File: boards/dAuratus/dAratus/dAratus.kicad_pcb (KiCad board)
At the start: 2 copper layers, 11 parts, among them SW1 SW_SPDT, U1 ADP7104ARDZ, U2 AVR128DB28-SOIC

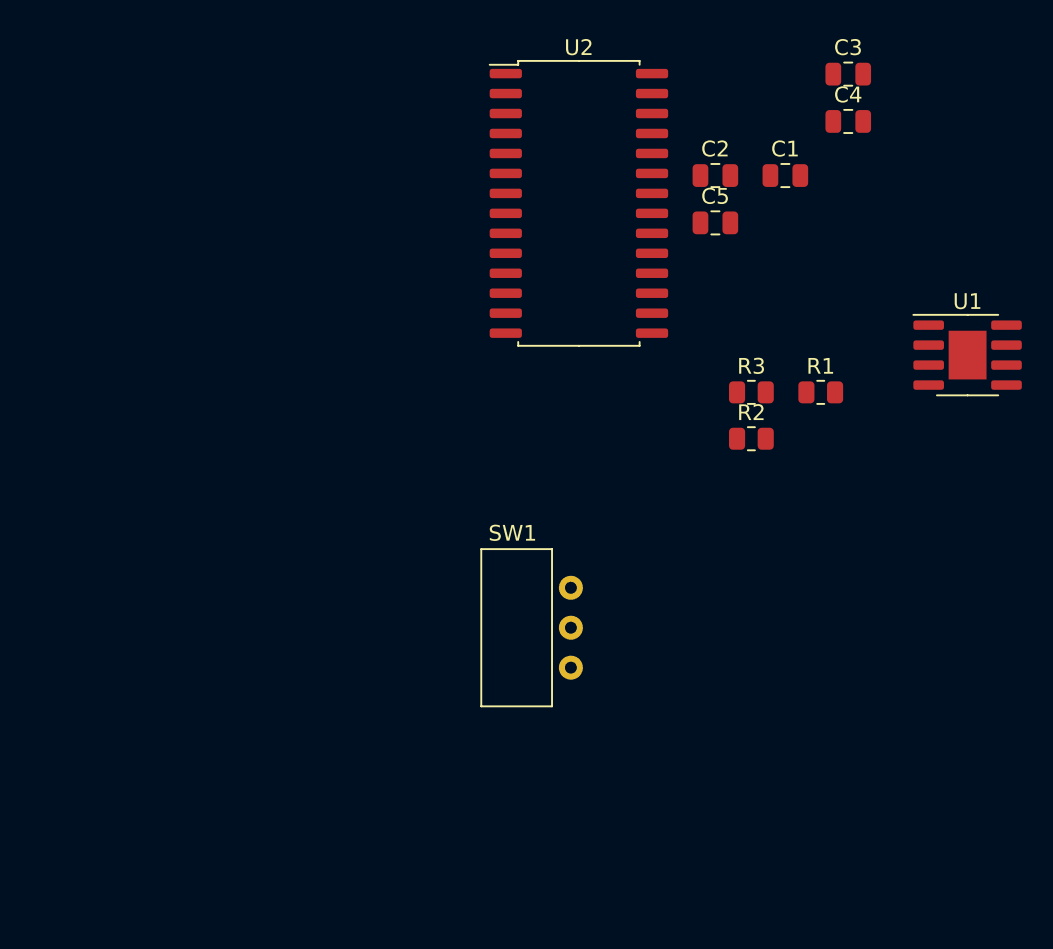
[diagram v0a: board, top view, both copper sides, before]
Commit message: Version 1.0 of fan control software.
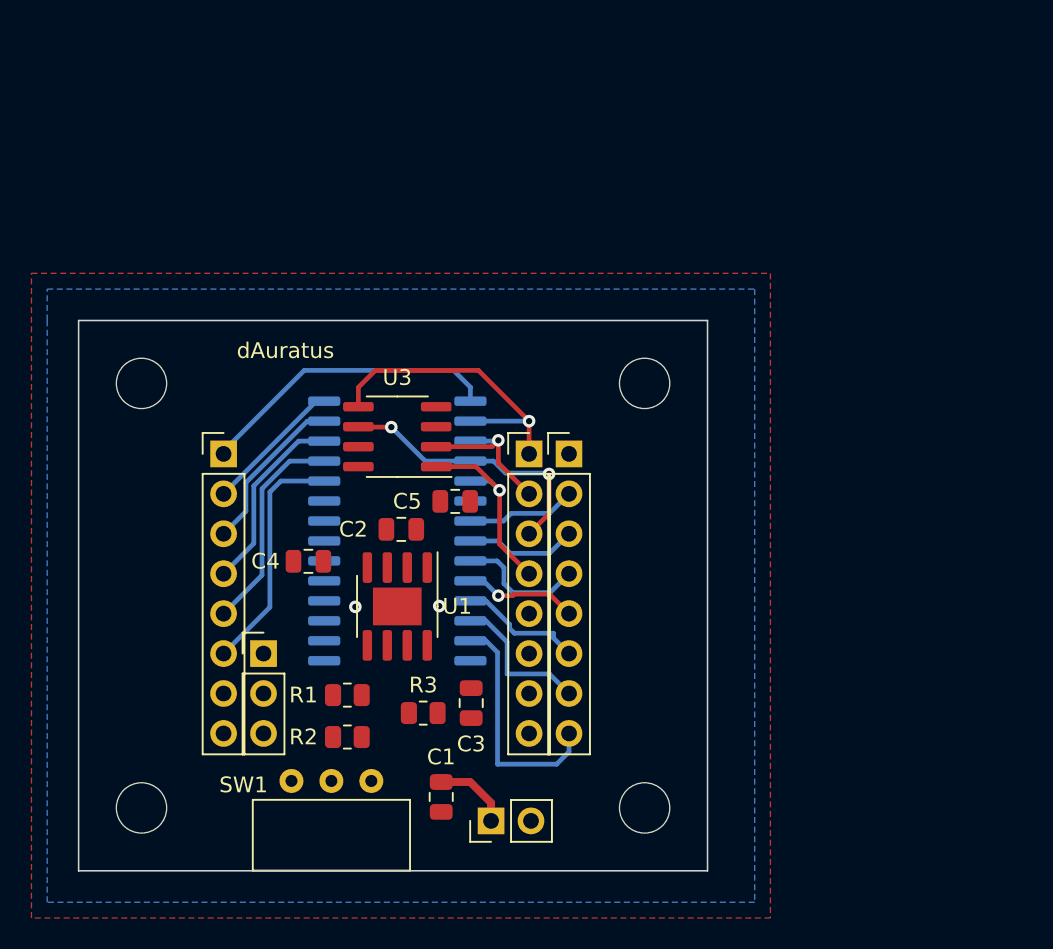
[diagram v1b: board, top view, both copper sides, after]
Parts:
- added H1: MountingHole, MountingHole:MountingHole_3.2mm_M3, F.Cu at (104.0, 104.0)
- added H2: MountingHole, MountingHole:MountingHole_3.2mm_M3, F.Cu at (136.0, 104.0)
- added H3: MountingHole, MountingHole:MountingHole_3.2mm_M3, F.Cu at (104.0, 131.0)
- added H4: MountingHole, MountingHole:MountingHole_3.2mm_M3, F.Cu at (136.0, 131.0)
- added J1: Conn_01x03_Male, Connector_PinHeader_2.54mm:PinHeader_1x03_P2.54mm_Vertical, F.Cu at (111.8, 121.2)
- added J2: Conn_01x08_Female, Connector_PinHeader_2.54mm:PinHeader_1x08_P2.54mm_Vertical, F.Cu at (131.2, 108.5)
- added J3: Conn_01x08_Female, Connector_PinHeader_2.54mm:PinHeader_1x08_P2.54mm_Vertical, F.Cu at (109.2, 108.5)
- added J4: Conn_01x08_Female, Connector_PinHeader_2.54mm:PinHeader_1x08_P2.54mm_Vertical, F.Cu at (128.7, 108.5)
- added J5: Conn_01x02_Male, Connector_PinHeader_2.54mm:PinHeader_1x02_P2.54mm_Vertical, F.Cu at (126.2, 131.8)
- added U3: AT25xxx, Package_SO:SOIC-8_3.9x4.9mm_P1.27mm, F.Cu at (120.3, 107.4)
- U2: moved to B.Cu
- moved C3 46.6 mm to (125.0, 124.3), turned to -90 degrees
- moved C1 45.2 mm to (123.1, 130.3), turned to -90 degrees
- moved C4 44.3 mm to (114.6, 115.3), turned to 180 degrees
- moved U1 39.6 mm to (120.3, 118.2), turned to -90 degrees
- moved R1 35.7 mm to (117.1, 123.8), turned to 180 degrees
- moved R2 31.9 mm to (117.1, 126.5), turned to 180 degrees
- moved C2 30.1 mm to (120.5, 113.3), turned to 180 degrees
- moved R3 29.2 mm to (121.9, 125.0), turned to 180 degrees
- moved C5 24.2 mm to (124.0, 111.5)
- moved U2 23.8 mm to (120.3, 113.4), turned to 180 degrees
- moved SW1 18.1 mm to (116.1, 129.3), turned to 180 degrees
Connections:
- net +3.3V renamed VDD
- U2 pad 1: unconnected-(U2-Pad1) -> /PA7
- U2 pad 10: unconnected-(U2-Pad10) -> /PD4
- U2 pad 11: unconnected-(U2-Pad11) -> /PD5
- U2 pad 12: unconnected-(U2-Pad12) -> /PD6
- U2 pad 13: unconnected-(U2-Pad13) -> /PD7
- U2 pad 19: unconnected-(U2-Pad19) -> /UPDI
- U2 pad 2: unconnected-(U2-Pad2) -> /MOSI
- U2 pad 22: unconnected-(U2-Pad22) -> /PA0
- U2 pad 23: unconnected-(U2-Pad23) -> /PA1
- U2 pad 24: unconnected-(U2-Pad24) -> /PA2
- U2 pad 25: unconnected-(U2-Pad25) -> /PA3
- U2 pad 26: unconnected-(U2-Pad26) -> /PA4
- U2 pad 27: unconnected-(U2-Pad27) -> /PA5
- U2 pad 28: unconnected-(U2-Pad28) -> /PA6
- U2 pad 3: unconnected-(U2-Pad3) -> /MISO
- U2 pad 4: unconnected-(U2-Pad4) -> /SCK
- U2 pad 5: unconnected-(U2-Pad5) -> /~{MEMSS}
- U2 pad 7: unconnected-(U2-Pad7) -> /PD1
- U2 pad 8: unconnected-(U2-Pad8) -> /PD2
- U2 pad 9: unconnected-(U2-Pad9) -> /PD3
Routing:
- net /MOSI: track 0.00 -> 19.7 mm, vias 0 -> 1
- net /PA7: track 0.00 -> 19.3 mm
- net /SCK: track 0.00 -> 17.8 mm, vias 0 -> 2
- net /PA2: track 0.00 -> 15.2 mm
- net /PD7: track 0.00 -> 15.2 mm
- net /PA3: track 0.00 -> 13.6 mm
- net /~{MEMSS}: track 0.00 -> 12.8 mm, vias 0 -> 1
- net /PA4: track 0.00 -> 12.0 mm
- net /PA5: track 0.00 -> 10.4 mm
- net /MISO: track 0.00 -> 10.1 mm, vias 0 -> 1
- net /PD6: track 0.00 -> 9.38 mm
- net /PA6: track 0.00 -> 8.84 mm
- net /PD3: track 0.00 -> 8.20 mm
- net /PD5: track 0.00 -> 7.99 mm
- net /PD4: track 0.00 -> 7.22 mm, vias 0 -> 1
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- added copper zone on B.Cu, net GND
- added copper zone on F.Cu, net GND
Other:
- board outline added: 40 x 35 mm
- board text added: "dAuratus"
